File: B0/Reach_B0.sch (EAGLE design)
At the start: 239 parts, among them IC1 TMC2100-LA, IC10 74AHC1G126DCK, IC11 74AHC1G126DCK, IC18 74AHC1G126DCK, IC2 TMC2100-LA, IC3 74AHC1G126DCK, IC4 74AHC1G126DCK, IC5 74AHC1G126DCK, IC6 74AHC1G126DCK, IC7 74AHC1G126DCK, IC8 TMC2100-LA, IC9 74AHC1G126DCK, P8 F-2X23-, P9 F-2X23-, Q2 AON6758, Q3 AON6758, U1 SN74AHC595PW, U10 RT8268, U11 PCA9685PW, U18 CAT24C256, U2 SN74AHC595PW, U3 MCP9600, U4 MCP9600, U5 MCP9600, U6 MCP9600, U7 SN74AHC595PW, X1 22-05-7028-02, X11 22-05-7028-02, X14 22-05-7048-04, X2 MSTBA4, X21 MSTBA2, X3 MSTBA2, X4 22-05-7028-02, X5 22-05-7028-02, X6 22-05-7048-04, X7 22-05-7028-02, X8 22-05-7048-04, X9 22-05-7028-02

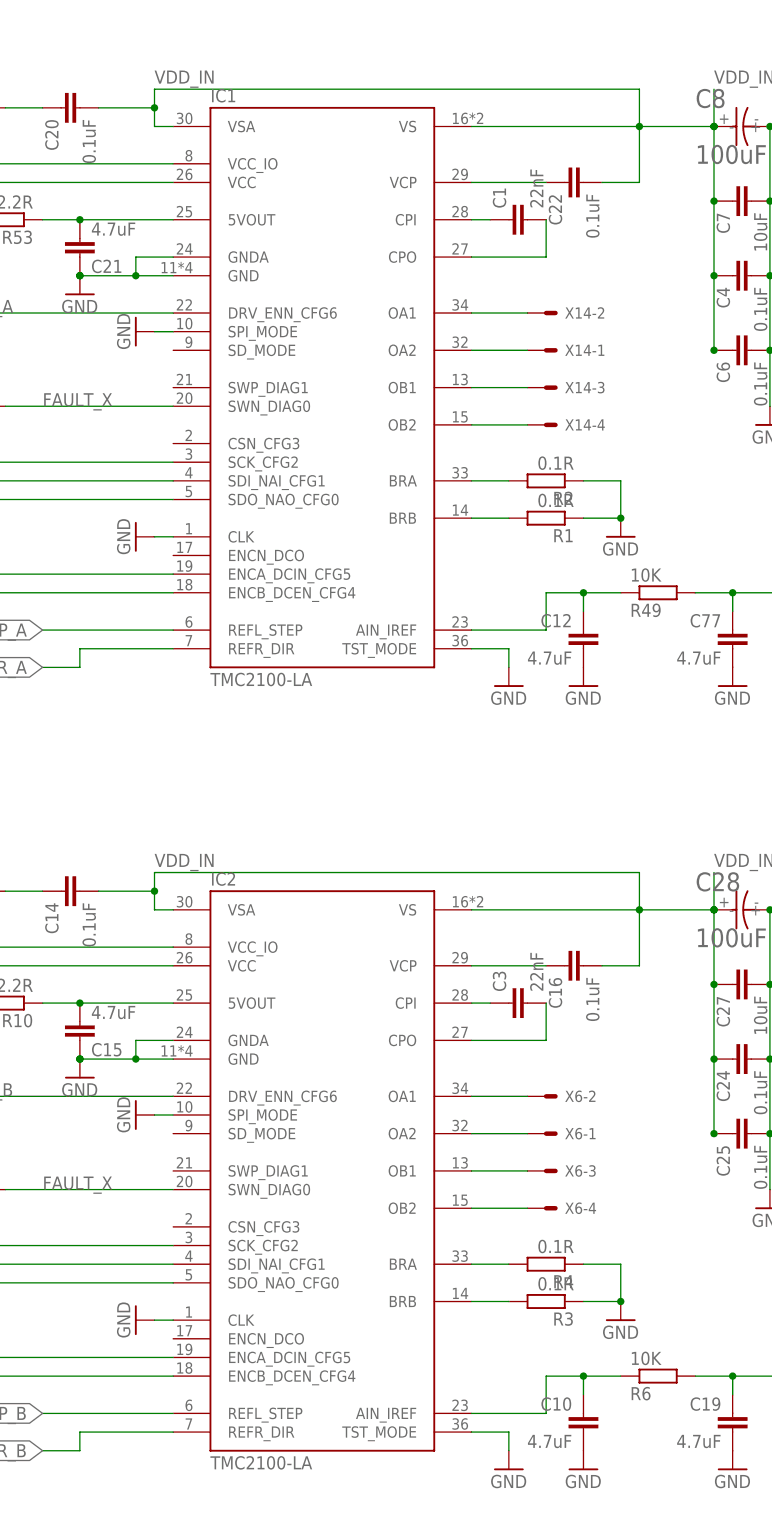
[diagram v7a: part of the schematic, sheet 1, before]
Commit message: TMC2130
Updated to TMC2130 for stepper driver, testing screw terminal layout for thermocouple connections (thermocouple connectors too expensive).
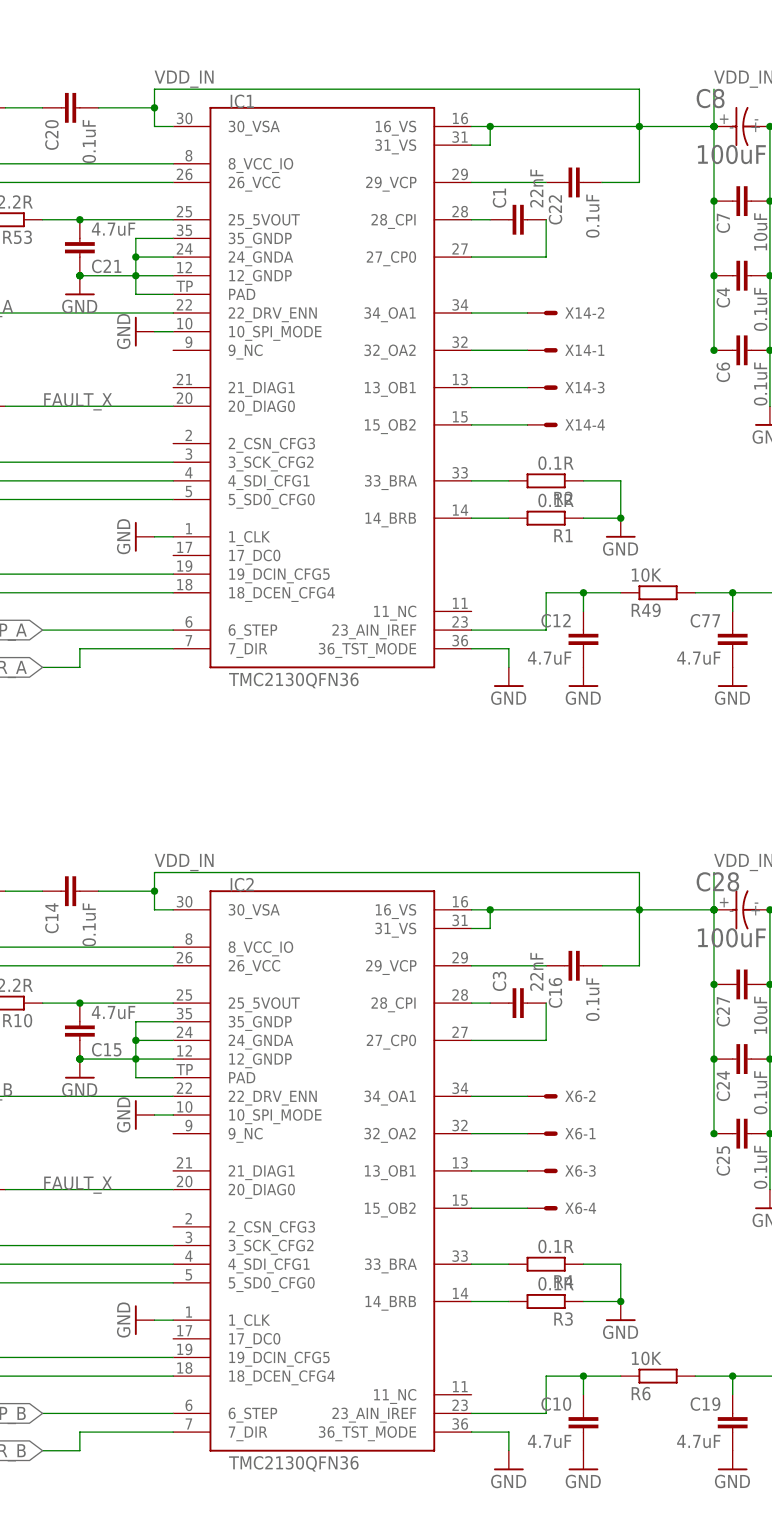
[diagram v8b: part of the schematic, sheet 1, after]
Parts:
- removed R61, R62: 0, SparkFun-Resistors:RESISTOR0805-RES
- removed XTC1: NEWPORT_THERMOCOUPLE_CONNECTORPCC-SMP-V, reach_custom:NEWPORT_THERMOCOUPLE_CONNECTORPCC-SMP-V
- added JP15: (no value), SparkFun-Connectors:M025MM
- IC1, IC2, IC8: value TMC2100-LA -> TMC2130QFN36; device we-chip:TMC2100-LA -> reach_custom:TMC2130QFN36
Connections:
- removed net N$51: R61.2, XTC1.P$3
- removed net N$73: R62.2, XTC1.P$4
- net +3V3: now also IC1.8_VCC_IO, IC2.8_VCC_IO, IC8.8_VCC_IO; no longer IC1.VCC_IO, IC2.VCC_IO, IC8.VCC_IO
- net B_A3: now also IC2.34_OA1; no longer IC2.OA1
- net B_A4: now also IC2.32_OA2; no longer IC2.OA2
- net B_B3: now also IC2.15_OB2; no longer IC2.OB2
- net B_B4: now also IC2.13_OB1; no longer IC2.OB1
- net C_A3: now also IC8.34_OA1; no longer IC8.OA1
- net C_A4: now also IC8.32_OA2; no longer IC8.OA2
- net C_B3: now also IC8.15_OB2; no longer IC8.OB2
- net C_B4: now also IC8.13_OB1; no longer IC8.OB1
- net DIR_A: now also IC1.7_DIR; no longer IC1.REFR_DIR
- net DIR_B: now also IC2.7_DIR; no longer IC2.REFR_DIR
- net DIR_C: now also IC8.7_DIR; no longer IC8.REFR_DIR
- net ENABLE_A: now also IC1.22_DRV_ENN; no longer IC1.DRV_ENN_CFG6
- net ENABLE_B: now also IC2.22_DRV_ENN; no longer IC2.DRV_ENN_CFG6
- net ENABLE_C: now also IC8.22_DRV_ENN; no longer IC8.DRV_ENN_CFG6
- net FAULT_X: now also IC1.20_DIAG0, IC2.20_DIAG0, IC8.20_DIAG0; no longer IC1.SWN_DIAG0, IC2.SWN_DIAG0, IC8.SWN_DIAG0
- net GND: now also IC1.10_SPI_MODE, IC1.12_GNDP, IC1.1_CLK, IC1.24_GNDA, IC1.35_GNDP, IC1.36_TST_MODE, IC1.PAD, IC2.10_SPI_MODE, IC2.12_GNDP, IC2.1_CLK, IC2.24_GNDA, IC2.35_GNDP, IC2.36_TST_MODE, IC2.PAD, IC8.10_SPI_MODE, IC8.12_GNDP, IC8.1_CLK, IC8.24_GNDA, IC8.35_GNDP, IC8.36_TST_MODE, IC8.PAD; no longer IC1.CLK, IC1.GND, IC1.GNDA, IC1.SPI_MODE, IC1.TST_MODE, IC2.CLK, IC2.GND, IC2.GNDA, IC2.SPI_MODE, IC2.TST_MODE, IC8.CLK, IC8.GND, IC8.GNDA, IC8.SPI_MODE, IC8.TST_MODE
- net GNDI: no longer R61.1, R62.1
- net N$1: now also IC2.27_CP0; no longer IC2.CPO
- net N$108: now also IC1.26_VCC; no longer IC1.VCC
- net N$14: now also JP15.1; no longer XTC1.P$1
- net N$15: now also JP15.2; no longer XTC1.P$2
- net N$16: now also IC1.28_CPI; no longer IC1.CPI
- net N$17: now also IC1.27_CP0; no longer IC1.CPO
- net N$18: now also IC1.14_BRB; no longer IC1.BRB
- net N$19: now also IC1.33_BRA; no longer IC1.BRA
- net N$2: now also IC2.14_BRB; no longer IC2.BRB
- net N$20: now also IC1.23_AIN_IREF; no longer IC1.AIN_IREF
- net N$22: now also IC2.23_AIN_IREF; no longer IC2.AIN_IREF
- net N$23: now also IC2.28_CPI; no longer IC2.CPI
- net N$24: now also IC2.25_5VOUT; no longer IC2.5VOUT
- net N$25: now also IC2.29_VCP; no longer IC2.VCP
- net N$26: now also IC2.18_DCEN_CFG4; no longer IC2.ENCB_DCEN_CFG4
- net N$27: now also IC2.19_DCIN_CFG5; no longer IC2.ENCA_DCIN_CFG5
- net N$3: now also IC2.33_BRA; no longer IC2.BRA
- net N$31: now also IC1.25_5VOUT; no longer IC1.5VOUT
- net N$33: now also IC1.29_VCP; no longer IC1.VCP
- net N$35: now also IC2.5_SD0_CFG0; no longer IC2.SDO_NAO_CFG0
- net N$36: now also IC2.26_VCC; no longer IC2.VCC
- net N$43: now also IC1.19_DCIN_CFG5; no longer IC1.ENCA_DCIN_CFG5
- net N$44: now also IC1.5_SD0_CFG0; no longer IC1.SDO_NAO_CFG0
- net N$52: now also IC8.27_CP0; no longer IC8.CPO
- net N$54: now also IC8.14_BRB; no longer IC8.BRB
- net N$55: now also IC8.33_BRA; no longer IC8.BRA
- net N$56: now also IC8.23_AIN_IREF; no longer IC8.AIN_IREF
- net N$57: now also IC8.28_CPI; no longer IC8.CPI
- net N$58: now also IC8.25_5VOUT; no longer IC8.5VOUT
- net N$59: now also IC8.29_VCP; no longer IC8.VCP
- net N$6: now also IC1.18_DCEN_CFG4; no longer IC1.ENCB_DCEN_CFG4
- net N$60: now also IC8.18_DCEN_CFG4; no longer IC8.ENCB_DCEN_CFG4
- net N$61: now also IC8.19_DCIN_CFG5; no longer IC8.ENCA_DCIN_CFG5
- net N$67: now also IC8.5_SD0_CFG0; no longer IC8.SDO_NAO_CFG0
- net N$68: now also IC8.26_VCC; no longer IC8.VCC
- net STEP_A: now also IC1.6_STEP; no longer IC1.REFL_STEP
- net STEP_B: now also IC2.6_STEP; no longer IC2.REFL_STEP
- net STEP_C: now also IC8.6_STEP; no longer IC8.REFL_STEP
- net VDD_IN: now also IC1.16_VS, IC1.30_VSA, IC1.31_VS, IC2.16_VS, IC2.30_VSA, IC2.31_VS, IC8.16_VS, IC8.30_VSA, IC8.31_VS; no longer IC1.VS, IC1.VSA, IC2.VS, IC2.VSA, IC8.VS, IC8.VSA
- net X_A1: now also IC1.34_OA1; no longer IC1.OA1
- net X_A2: now also IC1.32_OA2; no longer IC1.OA2
- net X_B1: now also IC1.13_OB1; no longer IC1.OB1
- net X_B2: now also IC1.15_OB2; no longer IC1.OB2
- net X_CFG1: now also IC1.4_SDI_CFG1; no longer IC1.SDI_NAI_CFG1
- net X_CFG2: now also IC1.3_SCK_CFG2; no longer IC1.SCK_CFG2
- net X_CFG3: now also IC2.3_SCK_CFG2; no longer IC2.SCK_CFG2
- net X_CFG4: now also IC2.4_SDI_CFG1; no longer IC2.SDI_NAI_CFG1
- net X_CFG5: now also IC8.3_SCK_CFG2; no longer IC8.SCK_CFG2
- net X_CFG6: now also IC8.4_SDI_CFG1; no longer IC8.SDI_NAI_CFG1
